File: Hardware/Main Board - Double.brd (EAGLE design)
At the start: 124.5 x 73.7 mm, 116 parts, among them J1 MICROMOD-2222-C, J10 MICRO-SD-PUSH-PUSH-EXT-PIN, J2 Vertical Qwiic Connector, J4 QWIIC_RIGHT_ANGLE, J5 CORTEX_JTAG_DEBUG_MINIMUM_PTH, J6 MICROMOD_FUNCTION_MAIN, J7 MICROMOD_FUNCTION_MAIN, Q1 3.1A/30V/105mΩ, U1 STG3856QTR, U2 MCP73831, U5 AP7361C-33

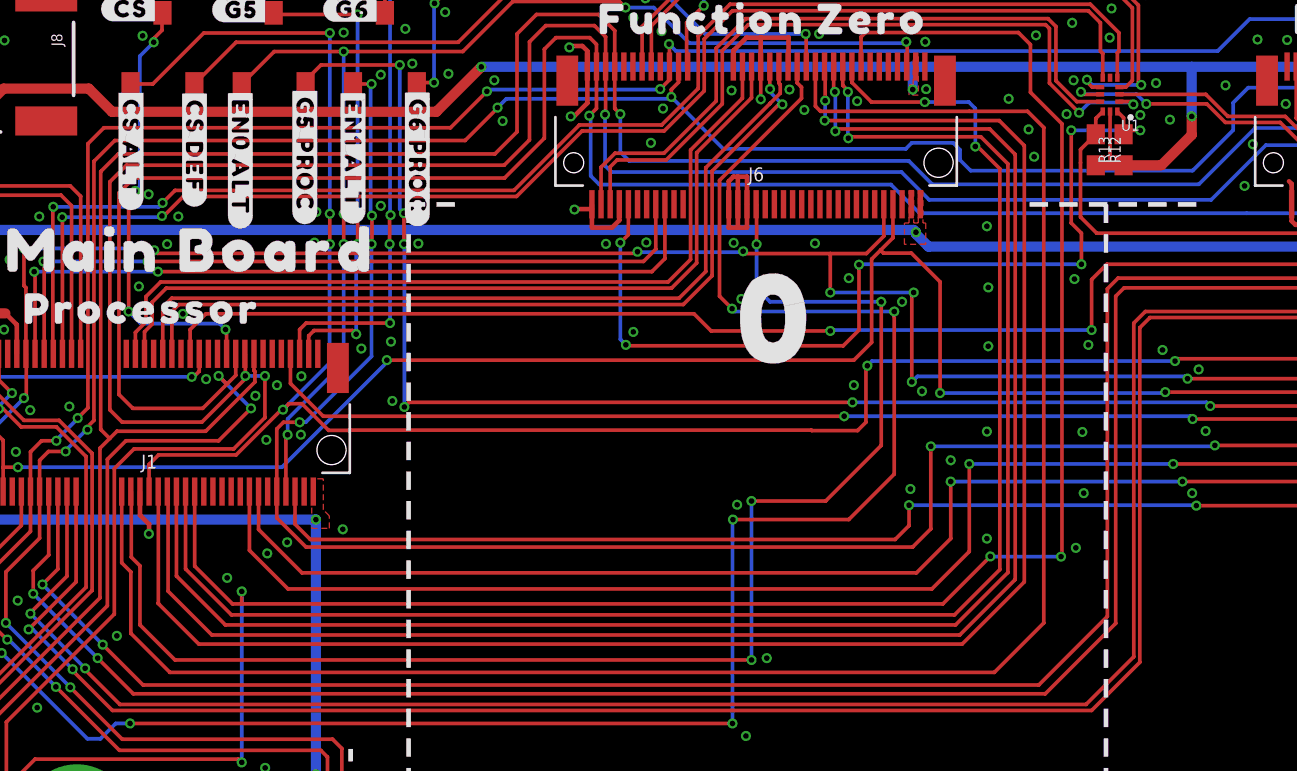
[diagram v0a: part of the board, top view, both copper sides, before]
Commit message: Fixes some vias, deletes value of jumper
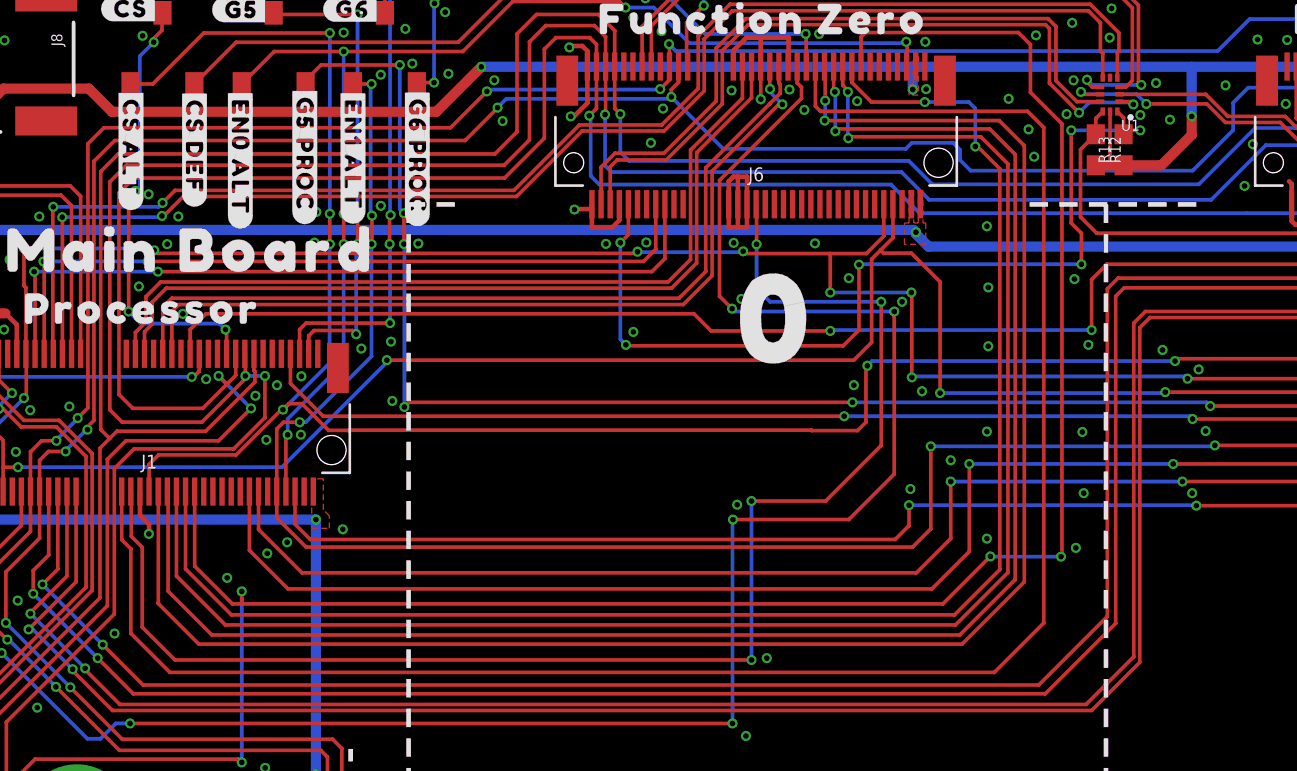
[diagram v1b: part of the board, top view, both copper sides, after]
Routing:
- net !BOOT!: track 135.5 -> 135.0 mm
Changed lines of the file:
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@@
 <setting verticaltext="up"/>
 </settings>
-<grid distance="0.01" unitdist="inch" unit="inch" style="dots" multiple="1" display="yes" altdistance="0.001" altunitdist="inch" altunit="inch"/>
+<grid distance="0.05" unitdist="inch" unit="inch" style="dots" multiple="1" display="yes" altdistance="0.005" altunitdist="inch" altunit="inch"/>
 <layers>
 <layer number="1" name="Top" color="4" fill="1" visible="yes" active="yes"/>
@@
 <layer number="19" name="Unrouted" color="6" fill="1" visible="yes" active="yes"/>
 <layer number="20" name="Dimension" color="15" fill="1" visible="yes" active="yes"/>
-<layer number="21" name="tPlace" color="16" fill="1" visible="no" active="yes"/>
-<layer number="22" name="bPlace" color="14" fill="1" visible="no" active="yes"/>
+<layer number="21" name="tPlace" color="16" fill="1" visible="yes" active="yes"/>
+<layer number="22" name="bPlace" color="14" fill="1" visible="yes" active="yes"/>
 <layer number="23" name="tOrigins" color="15" fill="1" visible="yes" active="yes"/>
 <layer number="24" name="bOrigins" color="15" fill="1" visible="yes" active="yes"/>
@@
 <layer number="37" name="tTest" color="7" fill="1" visible="no" active="yes"/>
 <layer number="38" name="bTest" color="7" fill="1" visible="no" active="yes"/>
-<layer number="39" name="tKeepout" color="4" fill="11" visible="yes" active="yes"/>
+<layer number="39" name="tKeepout" color="4" fill="11" visible="no" active="yes"/>
 <layer number="40" name="bKeepout" color="1" fill="11" visible="no" active="yes"/>
 <layer number="41" name="tRestrict" color="4" fill="10" visible="no" active="yes"/>
@@
 <via x="30.8102" y="54.9656" extent="1-16" drill="0.3048"/>
 <via x="22.4412" y="49.6852" extent="1-16" drill="0.3048"/>
-<via x="27.191" y="37.3154" extent="1-16" drill="0.3048"/>
+<via x="27.064" y="37.4424" extent="1-16" drill="0.3048"/>
 <via x="21.7554" y="39.2458" extent="1-16" drill="0.3048"/>
 <via x="20.0282" y="36.0454" extent="1-16" drill="0.3048"/>
@@
 <contactref element="J1" pad="34"/>
 <wire x1="27.956" y1="45.223" x2="27.9814" y2="45.1976" width="0.2032" layer="1"/>
-<wire x1="27.9814" y1="45.1976" x2="27.9814" y2="41.6265125" width="0.2032" layer="1"/>
-<wire x1="27.9814" y1="41.6265125" x2="28.456" y2="41.1519125" width="0.2032" layer="1"/>
-<wire x1="28.456" y1="41.1519125" x2="28.456" y2="37.913325" width="0.2032" layer="1"/>
+<wire x1="27.9814" y1="45.1976" x2="27.9814" y2="42.7695125" width="0.2032" layer="1"/>
+<wire x1="27.9814" y1="42.7695125" x2="28.583" y2="42.1679125" width="0.2032" layer="1"/>
+<wire x1="28.583" y1="42.1679125" x2="28.583" y2="37.786325" width="0.2032" layer="1"/>
 <contactref element="J6" pad="38"/>
 <wire x1="30.377525" y1="35.9918" x2="61.976" y2="35.9918" width="0.2032" layer="1"/>
@@
 <wire x1="61.976" y1="44.704" x2="66.04" y2="44.704" width="0.2032" layer="1"/>
 <wire x1="66.04" y1="44.704" x2="69.088" y2="47.752" width="0.2032" layer="1"/>
-<wire x1="28.456" y1="37.913325" x2="30.377525" y2="35.9918" width="0.2032" layer="1"/>
+<wire x1="28.583" y1="37.786325" x2="30.377525" y2="35.9918" width="0.2032" layer="1"/>
 <wire x1="69.088" y1="47.752" x2="69.088" y2="55.626" width="0.2032" layer="1"/>
 <via x="69.088" y="55.626" extent="1-16" drill="0.3048"/>
@@
 <via x="85.8774" y="51.4096" extent="1-16" drill="0.3048"/>
 <wire x1="85.8774" y1="51.4096" x2="85.7504" y2="51.5366" width="0.2032" layer="16"/>
-<wire x1="85.7504" y1="51.5366" x2="71.0692" y2="51.5366" width="0.2032" layer="16"/>
-<wire x1="71.0692" y1="51.5366" x2="70.7644" y2="51.2318" width="0.2032" layer="16"/>
-<via x="70.7644" y="51.2318" extent="1-16" drill="0.3048"/>
-<wire x1="70.7644" y1="56.0324" x2="70.7644" y2="51.2318" width="0.2032" layer="1"/>
-<wire x1="70.7644" y1="56.0324" x2="70.866" y2="56.134" width="0.2032" layer="1"/>
+<wire x1="85.7504" y1="51.5366" x2="70.8152" y2="51.5366" width="0.2032" layer="16"/>
+<wire x1="70.8152" y1="51.5366" x2="70.7644" y2="51.4858" width="0.2032" layer="16"/>
+<via x="70.7644" y="51.4858" extent="1-16" drill="0.3048"/>
+<wire x1="70.7644" y1="56.1086" x2="70.7644" y2="51.4858" width="0.2032" layer="1"/>
+<wire x1="70.7644" y1="56.1086" x2="70.739" y2="56.134" width="0.2032" layer="1"/>
 <wire x1="107.584" y1="57.3174" x2="101.6762" y2="51.4096" width="0.2032" layer="1"/>
-<via x="70.866" y="56.134" extent="1-16" drill="0.3048"/>
+<via x="70.739" y="56.134" extent="1-16" drill="0.3048"/>
 <wire x1="55.7276" y1="58.3692" x2="55.6387" y2="58.2803" width="0.2032" layer="1"/>
 <wire x1="55.6387" y1="58.2803" x2="29.40516875" y2="58.2803" width="0.2032" layer="1"/>
-<wire x1="70.866" y1="56.134" x2="66.294" y2="56.134" width="0.2032" layer="16"/>
+<wire x1="70.739" y1="56.134" x2="66.294" y2="56.134" width="0.2032" layer="16"/>
 <via x="66.294" y="56.134" extent="1-16" drill="0.3048"/>
 <wire x1="61.6458" y1="58.2676" x2="66.294" y2="58.2676" width="0.2032" layer="1"/>
@@
 <signal name="PWM0-PROCESSOR">
 <contactref element="J1" pad="32"/>
-<wire x1="27.456" y1="41.3178" x2="27.956" y2="40.8178" width="0.2032" layer="1"/>
-<wire x1="27.956" y1="40.8178" x2="27.956" y2="37.4522125" width="0.2032" layer="1"/>
+<wire x1="27.456" y1="42.5878" x2="27.956" y2="42.0878" width="0.2032" layer="1"/>
+<wire x1="27.956" y1="42.0878" x2="27.956" y2="37.4522125" width="0.2032" layer="1"/>
 <wire x1="77.9982" y1="38.0218125" x2="77.9982" y2="65.1764" width="0.2032" layer="1"/>
-<wire x1="27.456" y1="45.223" x2="27.456" y2="41.3178" width="0.2032" layer="1"/>
+<wire x1="27.456" y1="45.223" x2="27.456" y2="42.5878" width="0.2032" layer="1"/>
 <wire x1="27.956" y1="37.4522125" x2="30.0970125" y2="35.3112" width="0.2032" layer="1"/>
 <wire x1="30.0970125" y1="35.3112" x2="75.2875875" y2="35.3112" width="0.2032" layer="1"/>
 <wire x1="75.2875875" y1="35.3112" x2="77.9982" y2="38.0218125" width="0.2032" layer="1"/>
 <wire x1="77.9982" y1="65.1764" x2="77.1092" y2="66.0654" width="0.2032" layer="1"/>
-<wire x1="77.1092" y1="66.0654" x2="73.914" y2="66.0654" width="0.2032" layer="1"/>
-<wire x1="73.914" y1="66.0654" x2="65.7606" y2="66.0654" width="0.2032" layer="1"/>
+<wire x1="77.1092" y1="66.0654" x2="65.7606" y2="66.0654" width="0.2032" layer="1"/>
 <wire x1="65.7606" y1="66.0654" x2="65.48" y2="66.346" width="0.2032" layer="1"/>
 <contactref element="J6" pad="51"/>

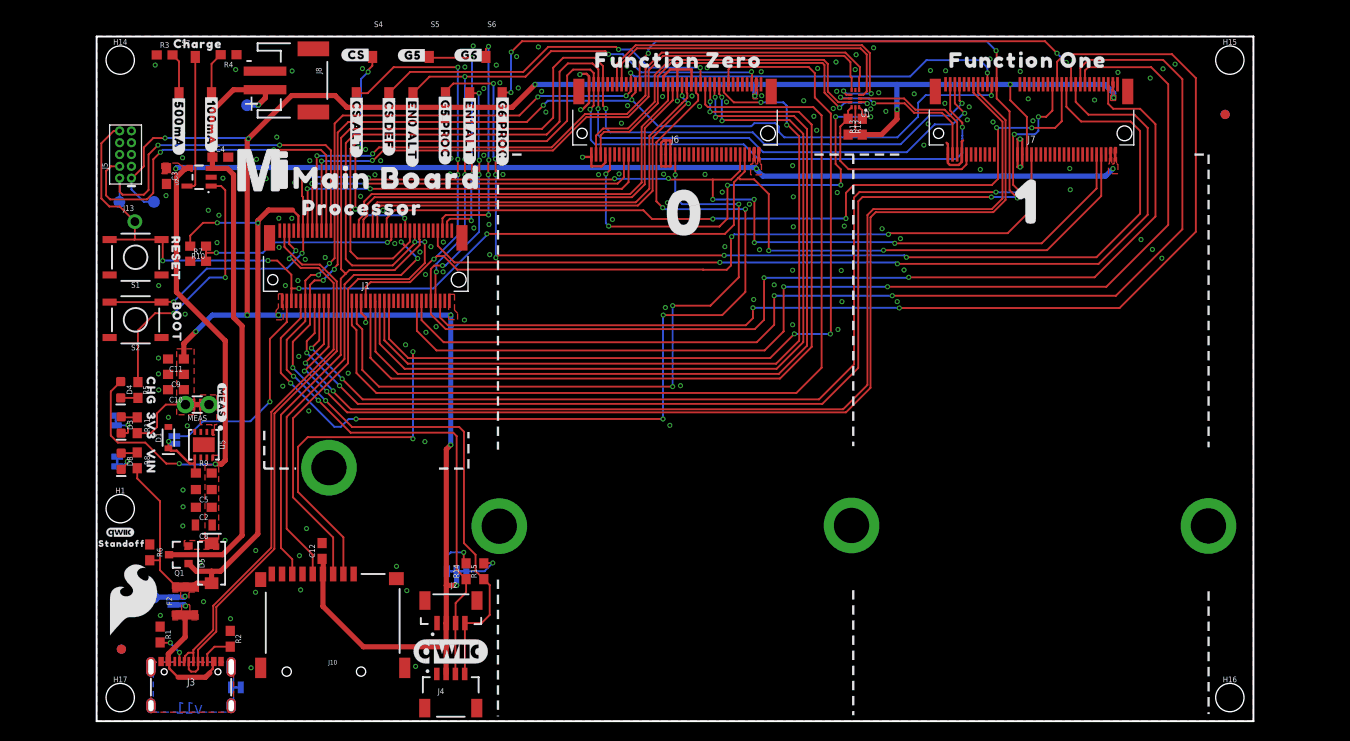
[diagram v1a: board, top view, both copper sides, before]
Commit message: Fixes ground pour in areas throughout, adds vias, updates net positioning and text layout in schematic
* Increases cap on output of VREG
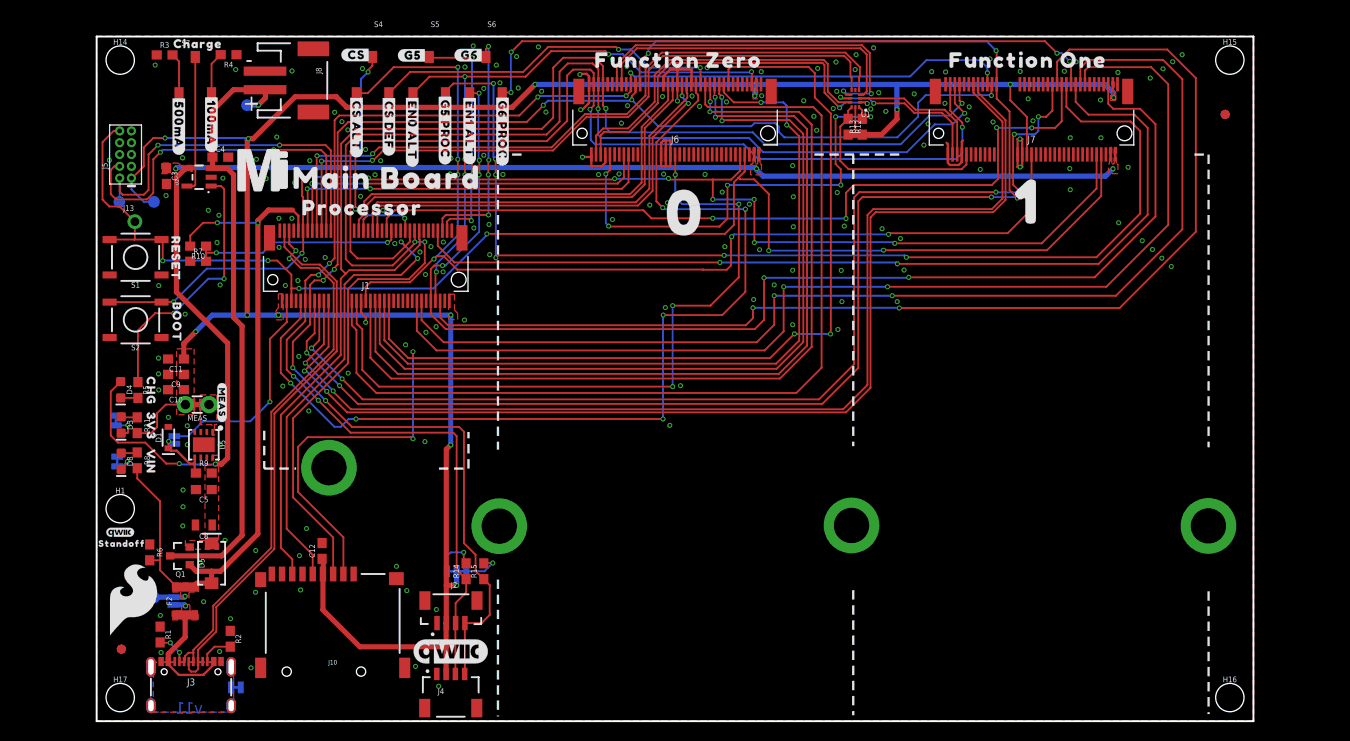
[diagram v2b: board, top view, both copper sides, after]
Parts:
- removed C2: 0.22uF, SparkFun-Capacitors:0603
- C11: value 0.22uF -> 2.2uF
- R8: value 4.7k -> 2.2k
- moved Q1 0.18 mm to (9.02, 17.8)
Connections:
- net N$7 renamed V_USB
- net GND: no longer C2.2
- net VCC: no longer C2.1
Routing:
- net SWDCK: track 40.9 -> 39.8 mm
- net GND: vias 171 -> 190

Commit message: Improves routing, snaps many parts to a much more sensible grid, removes some caps on INPUT and OUTPUT of VREG that were not necessary
* Adds another MEAS Jumper for 5V side
* Removes selection on charge circuit (500mA now only)
* Fixes chip select not being double routed corectly
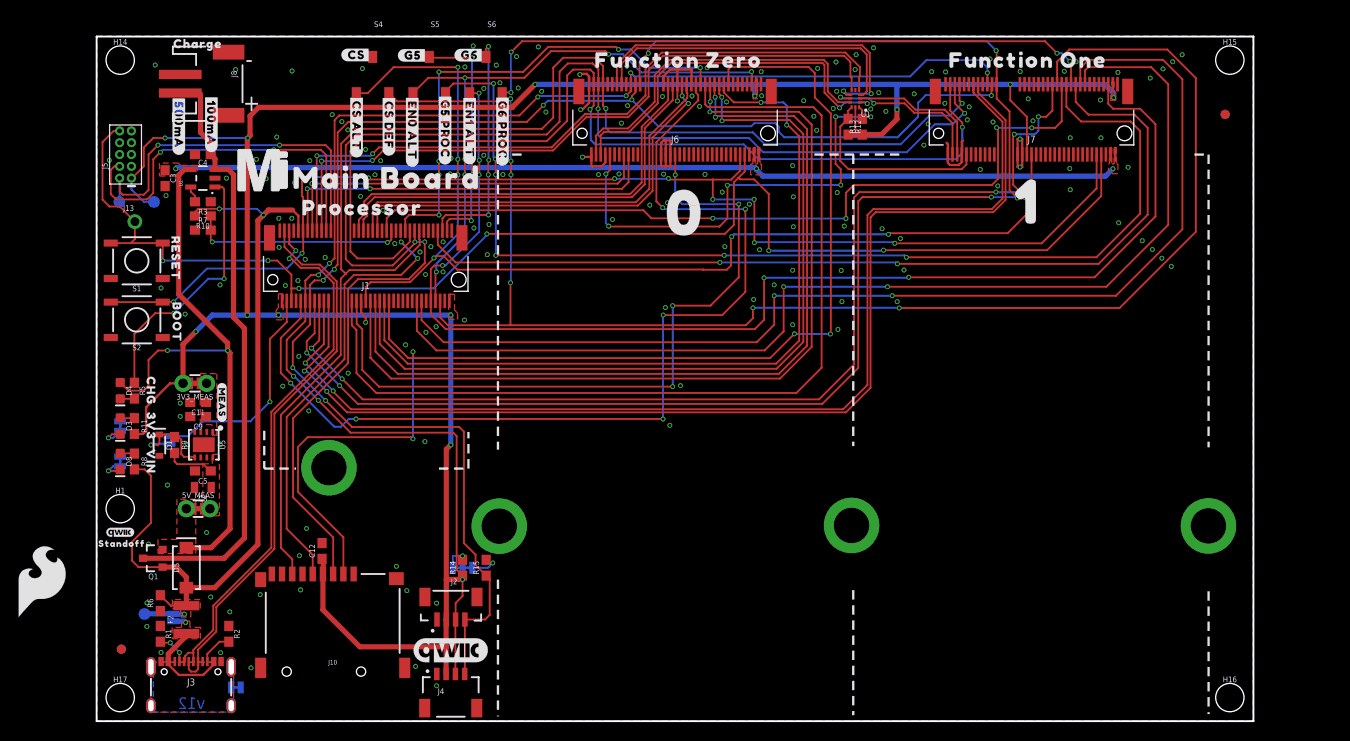
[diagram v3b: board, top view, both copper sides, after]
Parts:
- removed C10: 0.1uF, SparkFun-Capacitors:0603
- removed MEAS: JUMPER-COMBO_2_NC_TRACE, SparkFun-Jumpers:COMBO-JUMPER_2_NC_TRACE
- removed R4: 10k, SparkFun-Resistors:0603
- removed S7: DIPSWITCH-3-PIN, dip_switch:DIPSWITCH-SPDT
- added 3V3_MEAS, 5V_MEAS: JUMPER-COMBO_2_NC_TRACE, SparkFun-Jumpers:COMBO-JUMPER_2_NC_TRACE
- moved R3 16.3 mm to (11.4, 55.9), turned to 180 degrees
- moved U$24 10.0 mm to (-5.84, 15.0)
- moved J8 9.13 mm to (12.7, 68.6)
- moved TP3 7.29 mm to (8.89, 66.0)
- moved R6 5.58 mm to (6.86, 12.7), turned to 90 degrees
- moved C11 5.25 mm to (10.9, 34.3)
- moved C9 5.14 mm to (10.9, 32.8)
- moved R9 4.37 mm to (8.38, 29.7), turned to 270 degrees
- moved C8 4.04 mm to (11.4, 25.1)
- moved R7 3.39 mm to (11.4, 52.8)
- moved R10 3.29 mm to (11.4, 54.4)
- moved Q1 2.93 mm to (6.10, 17.5)
- moved D5 2.76 mm to (9.65, 16.5)
- moved TP4 2.05 mm to (5.16, 11.5)
- moved F2 2.01 mm to (9.65, 10.9)
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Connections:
- removed net !CS0!-PROC-JUMPER: J1.55, S4.P2
- removed net N$8: R3.2, S7.P1
- removed net N$9: R4.2, S7.P3
- new net !CS1!-PROC-JUMPER: S4.P2
- new net VCC_MEAS: 5V_MEAS.2, 5V_MEAS.4, C5.1, C8.1, R9.2, U5.8
- net !CS0!-PROCESSOR: now also J1.55; no longer S4.P3
- net !CS1!-PROCESSOR: now also S4.P3
- net 3.3V: now also 3V3_MEAS.2, 3V3_MEAS.4; no longer C10.1, C11.1, C9.1, MEAS.2, MEAS.4
- net GND: no longer C10.2, R4.1
- net N$1: now also 3V3_MEAS.1, 3V3_MEAS.3, C11.1, C9.1; no longer MEAS.1, MEAS.3
- net N$6: now also R3.2; no longer S7.P2
- net VCC: now also 5V_MEAS.1, 5V_MEAS.3; no longer C5.1, C8.1, R9.2, U5.8
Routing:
- net !CS1!-PROCESSOR: track 124.0 -> 162.0 mm, vias 2 -> 6
- net !CS0!-PROC-JUMPER: track 24.2 -> 0.00 mm, vias 4 -> 0
- net !CS0!-PROCESSOR: track 38.3 -> 52.4 mm, vias 2 -> 6
- net N$6: track 14.7 -> 1.78 mm
- net VCC: track 156.1 -> 164.7 mm
- net VIN: track 83.0 -> 89.6 mm
- net VCC_MEAS: track 0.00 -> 5.25 mm
- net 3.3V: track 259.2 -> 264.2 mm
- net N$9: track 4.55 -> 0.00 mm
- net N$8: track 4.40 -> 0.00 mm
- net 3.3V_EN_VE: track 6.71 -> 9.74 mm
- net N$11: track 4.88 -> 2.73 mm
- net V_BATT: track 66.6 -> 64.6 mm, vias 1 -> 0
- net V_USB: track 13.9 -> 11.9 mm
- net N$13: track 4.19 -> 3.27 mm
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- added copper zone on layer 1, net VCC_MEAS
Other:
- board text added: "v12"
- board text removed: "v11"

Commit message: Many more grid improvements
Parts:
- added J9: (no value), SparkFun-Connectors:1X01_NO_SILK
- moved I2C_PU 1.98 mm to (40.9, 15.2)
- moved J13 1.63 mm to (2.54, 53.3)
- moved R14 1.30 mm to (39.6, 15.2)
- moved R15 1.27 mm to (41.9, 15.2)
- moved J2 1.27 mm to (38.1, 8.89)
- moved C12 0.50 mm to (24.1, 18.8)
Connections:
- net GND: now also J9.1
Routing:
- net 3.3V: track 264.2 -> 267.9 mm
- net N$11: track 2.73 -> 3.52 mm
- net I2C_SCL: track 158.7 -> 157.9 mm
- net !RESET!: track 151.6 -> 151.1 mm
- net N$13: track 3.27 -> 3.78 mm
- net GND: vias 183 -> 184
